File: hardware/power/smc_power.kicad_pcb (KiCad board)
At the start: 4 copper layers, 100 x 100 mm, 104 parts, among them IC1 LM393DR2GH, J1 Screw_Terminal_01x02, J2 48V Input, J3 48V Output, J4 24V Brake Output, J5 Logic Output, Q1 P40B10SL, U1 TPS54360DDA, U2 AP2112K-3.3, U3 TPS54360DDA, U4 TPS16630PWPR, U5 MCP1416, U6 TL431B_C54830630, U7 L78L12_SOT89

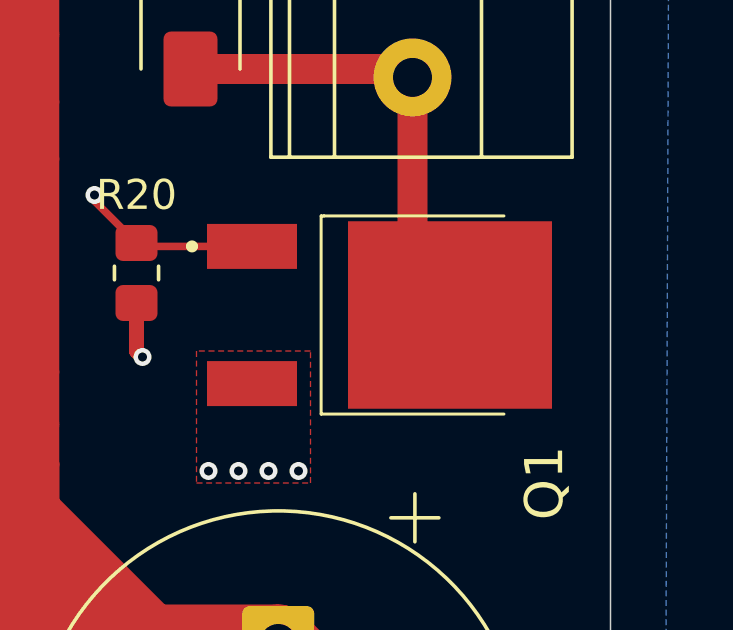
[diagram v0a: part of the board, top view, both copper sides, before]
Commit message: hw(power): Q1 drain tab 5x5 via array, refs #40
Co-Authored-By: Claude Opus 5.5 <noreply@anthropic.com>
Claude-Session: https://claude.ai/code/session_01SoMHYQYx4yCFML8vht6Kpa
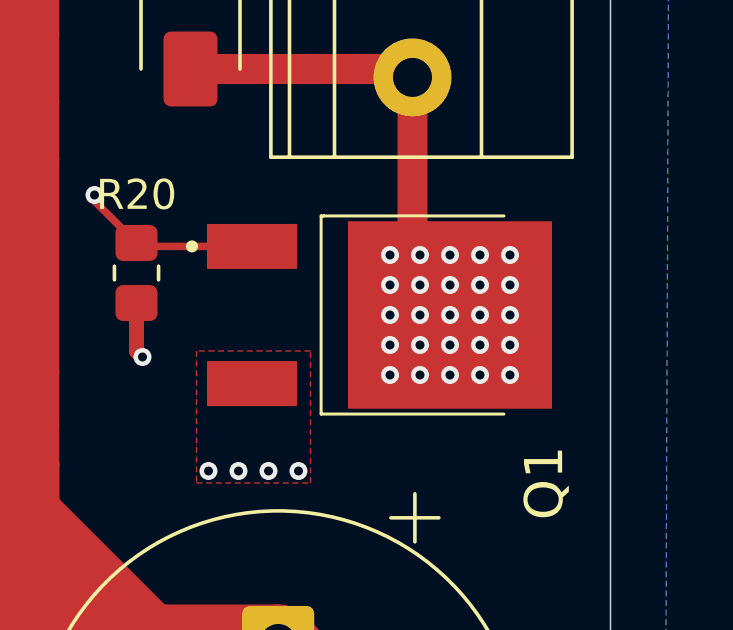
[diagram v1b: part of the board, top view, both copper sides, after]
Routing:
- net /CHOP_DRAIN: vias 0 -> 25

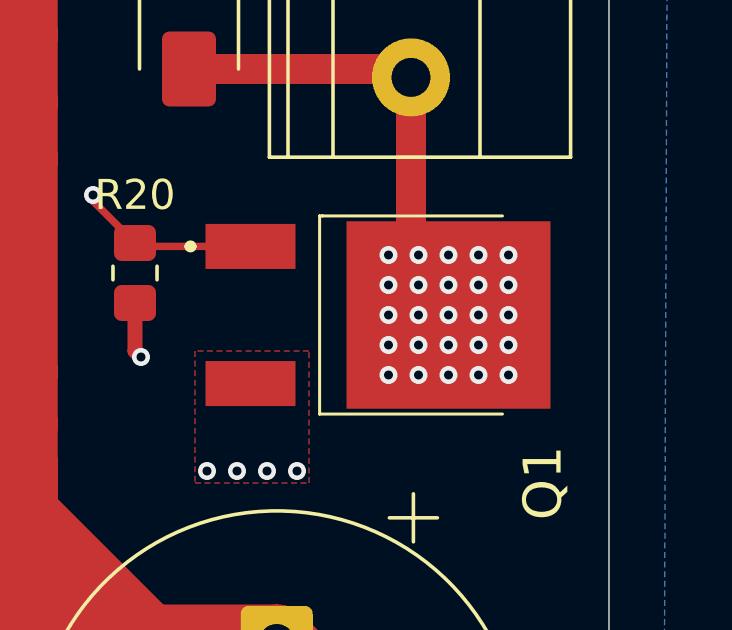
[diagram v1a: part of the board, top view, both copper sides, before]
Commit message: hw(power): CHOP_DRAIN copper under Q1 on B.Cu, refs #40
Co-Authored-By: Claude Opus 5.5 <noreply@anthropic.com>
Claude-Session: https://claude.ai/code/session_01SoMHYQYx4yCFML8vht6Kpa
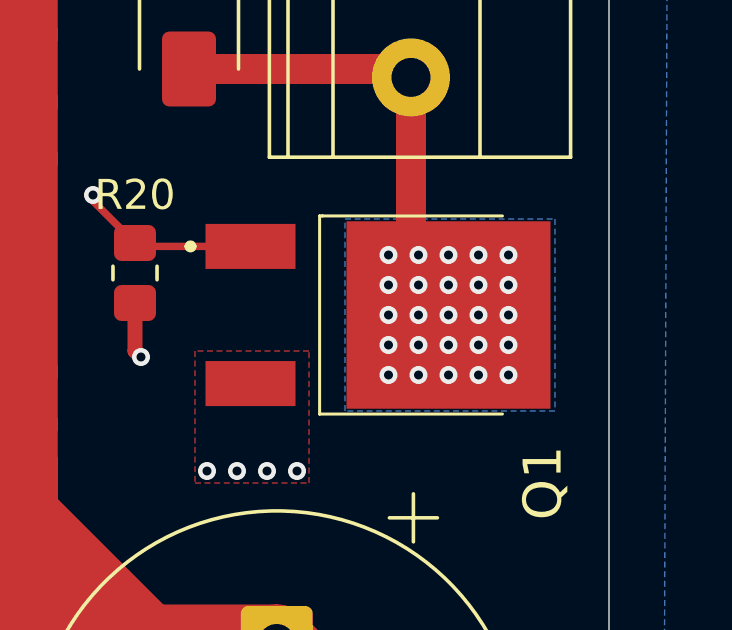
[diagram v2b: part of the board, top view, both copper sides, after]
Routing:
- added copper zone on B.Cu, net /CHOP_DRAIN
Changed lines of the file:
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@@
+	)
+	(zone
+		(net "/CHOP_DRAIN")
+		(layer "B.Cu")
+		(name "CHOP_DRAIN")
+		(hatch edge 0.5)
+		(priority 12)
+		(connect_pads yes
+			(clearance 0.5)
+		)
+		(min_thickness 0.25)
+		(fill
+			(thermal_gap 0.5)
+			(thermal_bridge_width 0.5)
+			(island_removal_mode 0)
+		)
+		(polygon
+			(pts
+				(xy 191.2 68.4) (xy 198.2 68.4) (xy 198.2 74.8) (xy 191.2 74.8)
+			)
+		)
 	)
 	(zone

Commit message: hw(power): U4 EP thermal vias, zones filled, refs #68
Co-Authored-By: Claude Opus 5.5 <noreply@anthropic.com>
Claude-Session: https://claude.ai/code/session_01SoMHYQYx4yCFML8vht6Kpa
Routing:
- net GND: vias 81 -> 87
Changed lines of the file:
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@@
 	)
 	(via
+		(at 144.4625 63.425)
+		(size 0.6)
+		(drill 0.3)
+		(layers "F.Cu" "B.Cu")
+		(net "GND")
+	)
+	(via
 		(at 131.1 62.5)
 		(size 0.6)
@@
 	)
 	(via
+		(at 143.4625 63.425)
+		(size 0.6)
+		(drill 0.3)
+		(layers "F.Cu" "B.Cu")
+		(net "GND")
+	)
+	(via
 		(at 176.35 25.075)
 		(size 0.6)
@@
 	)
 	(via
+		(at 143.4625 62.425)
+		(size 0.6)
+		(drill 0.3)
+		(layers "F.Cu" "B.Cu")
+		(net "GND")
+	)
+	(via
 		(at 104.8 32.4)
 		(size 0.6)
@@
 	)
 	(via
+		(at 144.4625 61.425)
+		(size 0.6)
+		(drill 0.3)
+		(layers "F.Cu" "B.Cu")
+		(net "GND")
+	)
+	(via
 		(at 187.6 76.8)
 		(size 0.6)
@@
 	)
 	(via
+		(at 144.4625 62.425)
+		(size 0.6)
+		(drill 0.3)
+		(layers "F.Cu" "B.Cu")
+		(net "GND")
+	)
+	(via
 		(at 186.975 49.725)
 		(size 0.6)
@@
 	)
 	(via
+		(at 143.4625 61.425)
+		(size 0.6)
+		(drill 0.3)
+		(layers "F.Cu" "B.Cu")
+		(net "GND")
+	)
+	(via
 		(at 186 22.35)
 		(size 0.6)
@@
 	)
 	(segment
-		(start 119.7 37.684062)
-		(end 116.615938 34.6)
-		(width 2.5)
+		(start 121.8 36.814214)
+		(end 119.585786 34.6)
+		(width 0.4)
+		(layer "F.Cu")
+		(net "+VM")
+	)
+	(segment
+		(start 121.7 53)
+		(end 121.8 52.9)
+		(width 0.4)
 		(layer "F.Cu")
 		(net "+VM")
@@
 	)
 	(segment
-		(start 116.615938 34.6)
-		(end 111.85 34.6)
-		(width 2.5)
-		(layer "F.Cu")
-		(net "+VM")
-	)
-	(segment
 		(start 180.375 62.25)
 		(end 180.375 59.375)
@@
 	)
 	(segment
+		(start 119.585786 34.6)
+		(end 111.85 34.6)
+		(width 0.4)
+		(layer "F.Cu")
+		(net "+VM")
+	)
+	(segment
 		(start 144.5 104.5)
 		(end 144.5 96.7)
@@
 	)
 	(segment
+		(start 121.8 52.9)
+		(end 121.8 36.814214)
+		(width 0.4)
+		(layer "F.Cu")
+		(net "+VM")
+	)
+	(segment
 		(start 193.425 46.625)
 		(end 191.65 46.625)
@@
 	)
 	(segment
-		(start 119.7 51.7)
-		(end 119.7 37.684062)
-		(width 2.5)
-		(layer "F.Cu")
-		(net "+VM")
-	)
-	(segment
 		(start 180.375 76.575)
 		(end 180.375 78.275)
@@
 	)
 	(via
-		(at 119.7 51.7)
+		(at 121.7 53)
 		(size 0.6)
 		(drill 0.3)
@@
 	)
 	(segment
-		(start 137.315938 98.7)
-		(end 141.4 98.7)
-		(width 2.5)
+		(start 121.661578 53.461578)
+		(end 121.8 53.6)
+		(width 0.4)
+		(layer "B.Cu")
+		(net "+VM")
+	)
+	(segment
+		(start 121.8 80.214214)
+		(end 138.185786 96.6)
+		(width 0.4)
 		(layer "B.Cu")
 		(net "+VM")
 	)
 	(segment
-		(start 141.4 98.7)
+		(start 139.3 96.6)
 		(end 144.5 101.8)
-		(width 2.5)
+		(width 0.4)
 		(layer "B.Cu")
 		(net "+VM")
 	)
 	(segment
-		(start 144.5 101.8)
-		(end 144.5 104.5)
-		(width 2.5)
+		(start 121.8 53.6)
+		(end 121.8 80.214214)
+		(width 0.4)
 		(layer "B.Cu")
 		(net "+VM")
 	)
 	(segment
-		(start 119.7 81.084062)
-		(end 137.315938 98.7)
+		(start 144.5 101.8)
+		(end 144.5 104.5)
 		(width 2.5)
 		(layer "B.Cu")
@@
 	)
 	(segment
-		(start 119.7 51.7)
-		(end 119.7 81.084062)
-		(width 2.5)
+		(start 121.661578 53.038422)
+		(end 121.661578 53.461578)
+		(width 0.4)
+		(layer "B.Cu")
+		(net "+VM")
+	)
+	(segment
+		(start 121.7 53)
+		(end 121.661578 53.038422)
+		(width 0.4)
+		(layer "B.Cu")
+		(net "+VM")
+	)
+	(segment
+		(start 138.185786 96.6)
+		(end 139.3 96.6)
+		(width 0.4)
 		(layer "B.Cu")
 		(net "+VM")
@@
 	)
 	(segment
-		(start 117 30.6)
-		(end 111.85 30.6)
-		(width 2.5)
+		(start 122.8 50.697679)
+		(end 122.8 36.4)
+		(width 0.4)
 		(layer "F.Cu")
 		(net "+48V")
@@
 	)
 	(segment
-		(start 122.8 51.8)
-		(end 122.8 36.4)
-		(width 2.5)
+		(start 117 30.6)
+		(end 111.85 30.6)
+		(width 0.4)
 		(layer "F.Cu")
 		(net "+48V")
 	)
 	(segment
-		(start 168.593334 105.79)
-		(end 171.993334 105.79)
-		(width 2.5)
+		(start 122.9 50.797679)
+		(end 122.8 50.697679)
+		(width 0.4)
 		(layer "F.Cu")
 		(net "+48V")
 	)
 	(segment
-		(start 122.8 36.4)
-		(end 117 30.6)
+		(start 168.593334 105.79)
+		(end 171.993334 105.79)
 		(width 2.5)
 		(layer "F.Cu")
@@
 		(net "+48V")
 	)
+	(segment
+		(start 122.8 36.4)
+		(end 117 30.6)
+		(width 0.4)
+		(layer "F.Cu")
+		(net "+48V")
+	)
 	(via
 		(at 169.8 100.4)
@@
 	)
 	(via
-		(at 122.8 51.8)
+		(at 122.9 50.797679)
 		(size 0.6)
 		(drill 0.3)
@@
 	)
 	(segment
-		(start 165 95.6)
-		(end 169.8 100.4)
-		(width 2.5)
+		(start 122.8 79.8)
+		(end 138.6 95.6)
+		(width 0.4)
 		(layer "B.Cu")
 		(net "+48V")
 	)
 	(segment
-		(start 122.8 79.8)
-		(end 138.6 95.6)
-		(width 2.5)
+		(start 122.8 50.897679)
+		(end 122.8 79.8)
+		(width 0.4)
+		(layer "B.Cu")
+		(net "+48V")
+	)
+	(segment
+		(start 122.9 50.797679)
+		(end 122.8 50.897679)
+		(width 0.4)
 		(layer "B.Cu")
 		(net "+48V")
@@
 		(start 138.6 95.6)
 		(end 165 95.6)
-		(width 2.5)
+		(width 0.4)
 		(layer "B.Cu")
 		(net "+48V")
 	)
 	(segment
-		(start 122.8 51.8)
-		(end 122.8 79.8)
-		(width 2.5)
+		(start 165 95.6)
+		(end 169.8 100.4)
+		(width 0.4)
 		(layer "B.Cu")
 		(net "+48V")
@@
 		)
 		(min_thickness 0.25)
-		(fill
+		(fill yes
 			(thermal_gap 0.5)
 			(thermal_bridge_width 0.5)
@@
 		)
 		(min_thickness 0.25)
-		(fill
+		(fill yes
 			(thermal_gap 0.5)
 			(thermal_bridge_width 0.5)
@@
 		)
 		(min_thickness 0.25)
-		(fill
+		(fill yes
 			(thermal_gap 0.5)
 			(thermal_bridge_width 0.5)
@@
 		)
 		(min_thickness 0.25)
-		(fill
+		(fill yes
 			(thermal_gap 0.5)
 			(thermal_bridge_width 0.5)
@@
 		)
 		(min_thickness 0.25)
-		(fill
+		(fill yes
 			(thermal_gap 0.5)
 			(thermal_bridge_width 0.5)
@@
 		)
 		(min_thickness 0.25)
-		(fill
+		(fill yes
 			(thermal_gap 0.5)
 			(thermal_bridge_width 0.5)
@@
 		)
 		(min_thickness 0.25)
-		(fill
+		(fill yes
 			(thermal_gap 0.5)
 			(thermal_bridge_width 0.5)
@@
 		)
 		(min_thickness 0.25)
-		(fill
+		(fill yes
 			(thermal_gap 0.5)
 			(thermal_bridge_width 0.5)
@@
 		)
 		(min_thickness 0.25)
-		(fill
+		(fill yes
 			(thermal_gap 0.5)
 			(thermal_bridge_width 0.5)
@@
 		)
 		(min_thickness 0.25)
-		(fill
+		(fill yes
 			(thermal_gap 0.5)
 			(thermal_bridge_width 0.5)
@@
 		)
 		(min_thickness 0.25)
-		(fill
+		(fill yes
 			(thermal_gap 0.5)
 			(thermal_bridge_width 0.5)
@@
 		)
 		(min_thickness 0.25)
-		(fill
+		(fill yes
 			(thermal_gap 0.5)
 			(thermal_bridge_width 0.5)
@@
 		)
 		(min_thickness 0.25)
-		(fill
+		(fill yes
 			(thermal_gap 0.5)
 			(thermal_bridge_width 0.5)
@@
 		)
 		(min_thickness 0.25)
-		(fill
+		(fill yes
 			(thermal_gap 0.5)
 			(thermal_bridge_width 0.5)
@@
 		)
 		(min_thickness 0.25)
-		(fill
+		(fill yes
 			(thermal_gap 0.5)
 			(thermal_bridge_width 0.5)
@@
 		)
 		(min_thickness 0.25)
-		(fill
+		(fill yes
 			(thermal_gap 0.5)
 			(thermal_bridge_width 0.5)
